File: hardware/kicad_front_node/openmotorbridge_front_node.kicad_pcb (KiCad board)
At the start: 2 copper layers, 82 x 50 mm, 54 parts, among them J1 12V_KL15_GND, J10 12V_QI_POWER, J11 12V_AUX_LIGHT, J12 QWIIC_I2C, J2 CAN_H_L_GND, J3 HANDLEBAR_MULTI_BTN, J4 USB_UPSTREAM_HOST, J5 USB_DN1_PHONE_PD20W, J5_MP3 USB_DN3_GLOVEBOX_PD20W, J6 USB_DN2_CP2AA_PIGTAIL, J6_AUX USB_DN4_COCKPIT_AUX, J7 USB-C_SERVICE, J8 ACTION_CAM_5V_PWR, J9 MIRROR_BSD_LEDS, K1 CPC1017N_CAN_RELAY, Q1 DMN63D8_BSD_MOSFET, Q2 TPS1H100_AUX_LIGHT, SW1 BOOT, SW2 RESET, U1 ESP32-S3-WROOM-1U, U2 USB2514Bi-AEZG, U3 TPS54302_5V_BUCK, U4 TPS2051B_PORT2_GATE, U5 SW3526_USB_PD1_20W, U6 TCAN334G_CAN, U7 TLV75533P_3V3_LDO, U8 SW3526_USB_PD3_20W, Y1 24.000MHz

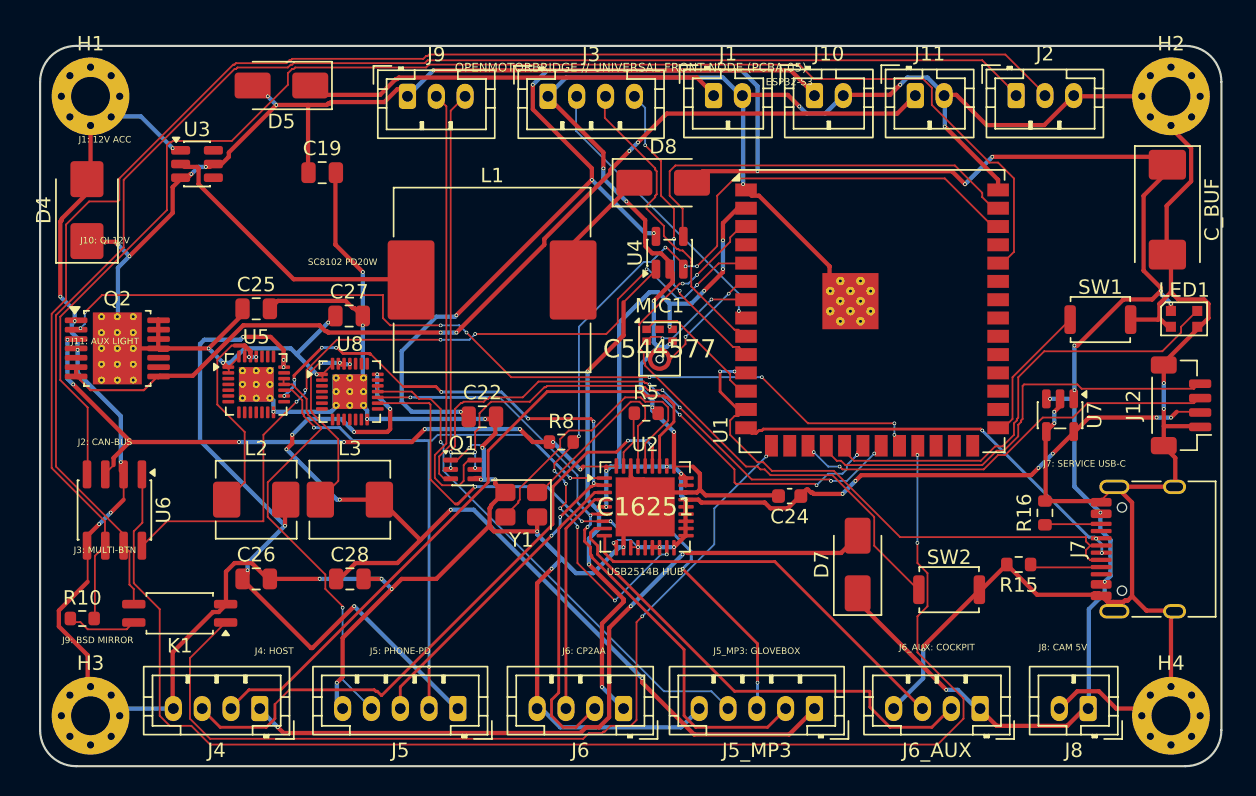
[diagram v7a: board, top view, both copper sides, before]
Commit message: hardware: update routed front node PCB and regenerate manufacturing packages
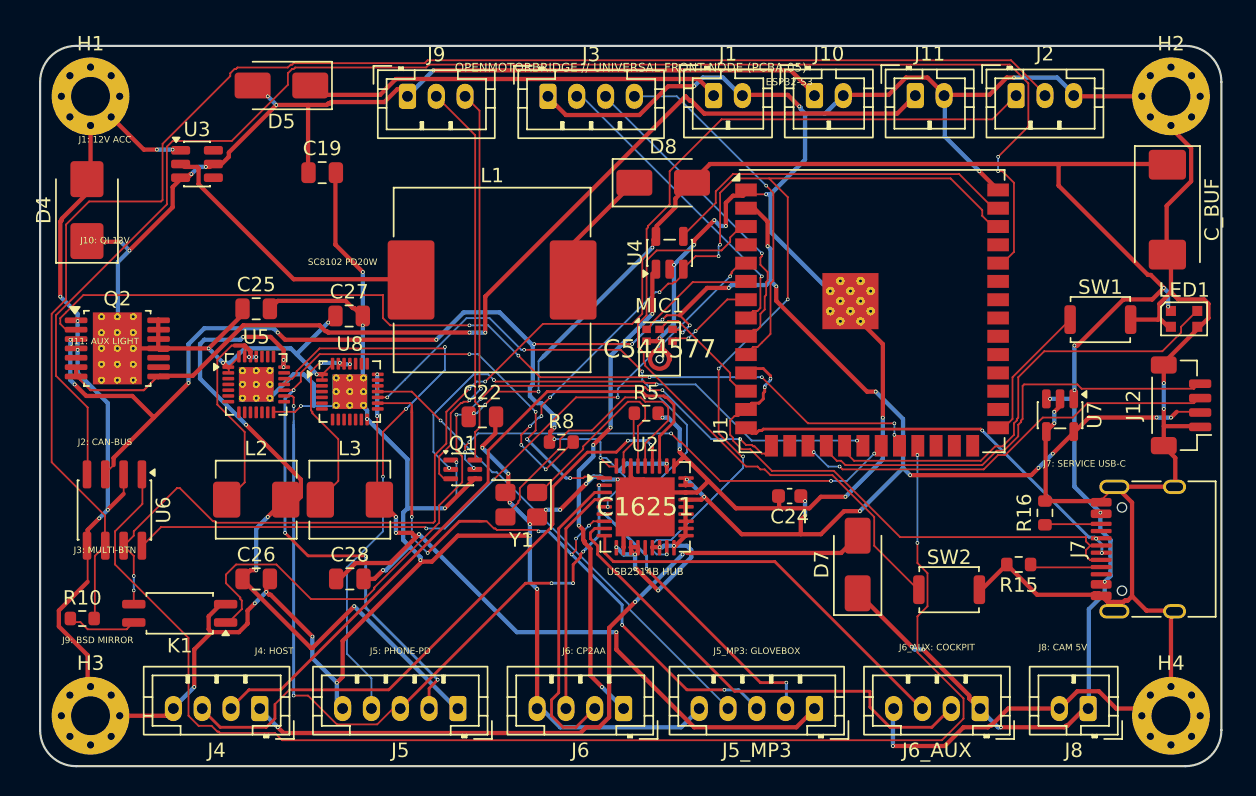
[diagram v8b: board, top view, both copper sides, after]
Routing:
- net VCC_3V3: track 135.3 -> 178.3 mm, vias 27 -> 35
- net VCC_5V: track 168.4 -> 130.1 mm, vias 16 -> 14
- net GND: track 412.8 -> 447.4 mm, vias 38 -> 49
- net OTTOCAST_FAULT_N: track 65.5 -> 85.1 mm, vias 10 -> 12
- net USB_DN1_DM: track 44.4 -> 58.7 mm, vias 3 -> 8
- net VBUS_PD3_OUT: track 67.6 -> 54.4 mm, vias 8 -> 6
- net USB_DN1_CC: track 28.9 -> 41.1 mm, vias 1 -> 3
- net USB_DN3_DM: track 45.3 -> 56.0 mm, vias 3 -> 6
- net CAN_H: track 100.2 -> 90.2 mm, vias 0 -> 4
- net CAN_TERM_EN: track 62.8 -> 55.3 mm, vias 2 -> 4
- net CAN_SILENT: track 57.1 -> 50.6 mm, vias 6 -> 4
- net TWAI_RX: track 98.8 -> 104.7 mm, vias 0 -> 2
- net BSD_LEFT_N: track 31.5 -> 26.7 mm
- net USB_DN3_DP: track 43.5 -> 48.1 mm, vias 5 -> 8
- net OTTOCAST_PWR_EN: track 29.3 -> 25.2 mm
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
